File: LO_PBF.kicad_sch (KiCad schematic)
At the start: 10 parts, among them J1 Conn_Coaxial, J2 Conn_Coaxial

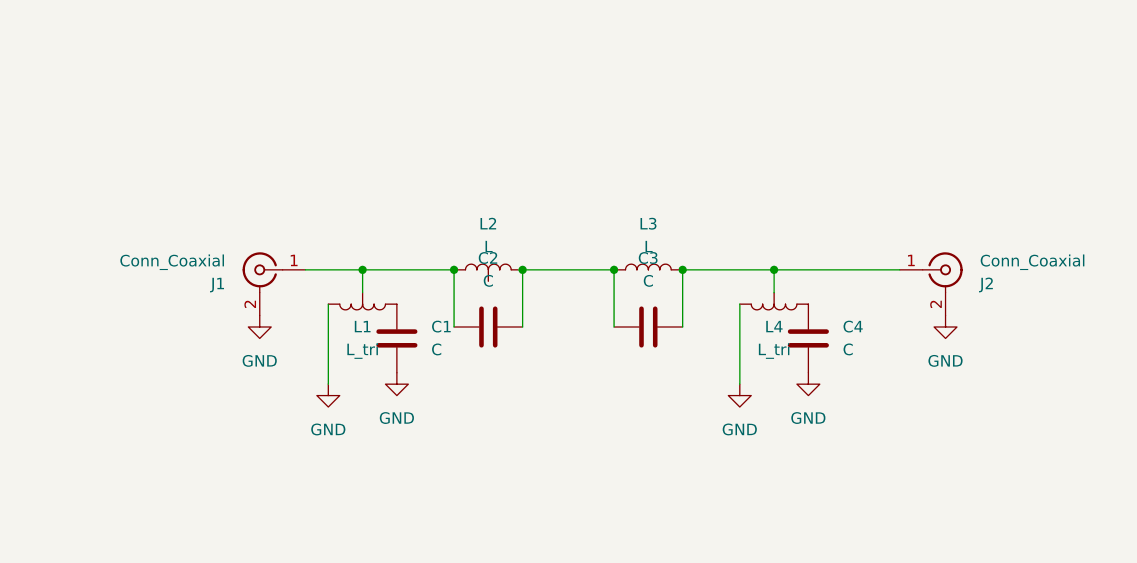
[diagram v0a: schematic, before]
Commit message: like ordered to JLCPCB
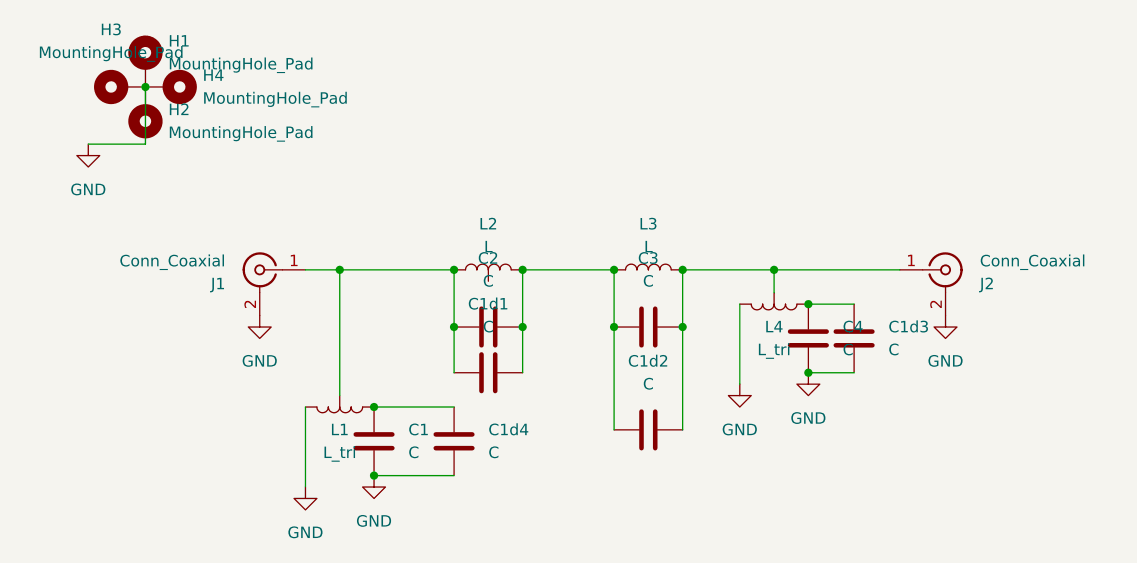
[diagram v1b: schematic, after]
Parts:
- added C1d1, C1d2, C1d3, C1d4: C, 3_Condensatori:C_1812_multiplo, symbol Device:C
- added H1, H2, H3, H4: MountingHole_Pad, MountingHole:MountingHole_3.2mm_M3_Pad, symbol Mechanical:MountingHole_Pad
- J1, J2: footprint 2_Connettori:PL-SO-239-2-hole-one-gnd -> 1_Induttori:coax_solder
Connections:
- net GND: now also C1d3.1, C1d4.2, H1.1, H2.1, H3.1, H4.1
- net at C4.1, L4.1: now also C1d3.2
- net at C2.1, C3.2, L2.2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: now also C1d1.2, C1d2.1
- net at C2.2, J1.1 (In), L1.2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: now also C1d1.1
- net at C3.1, J2.1 (In), L3.2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: now also C1d2.2
- net at C1.1, L1.1: now also C1d4.1
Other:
- moved on the sheet: C1, L1
